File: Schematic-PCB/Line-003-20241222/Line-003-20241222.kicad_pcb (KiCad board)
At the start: 4 copper layers, 196 x 193.6 mm, 245 parts, among them J1 VIN, J2 Conn_MD, U47 LM393, U48 LM393, U49 LM393, U50 LM393, U51 LM393, U52 LM393, U53 LM393, U54 LM393, U55 LM393, U56 LM393, U57 LM393, U58 LM393, U59 LM393, U60 LM393, U61 LM393, U62 ATmega2560 Pro Board

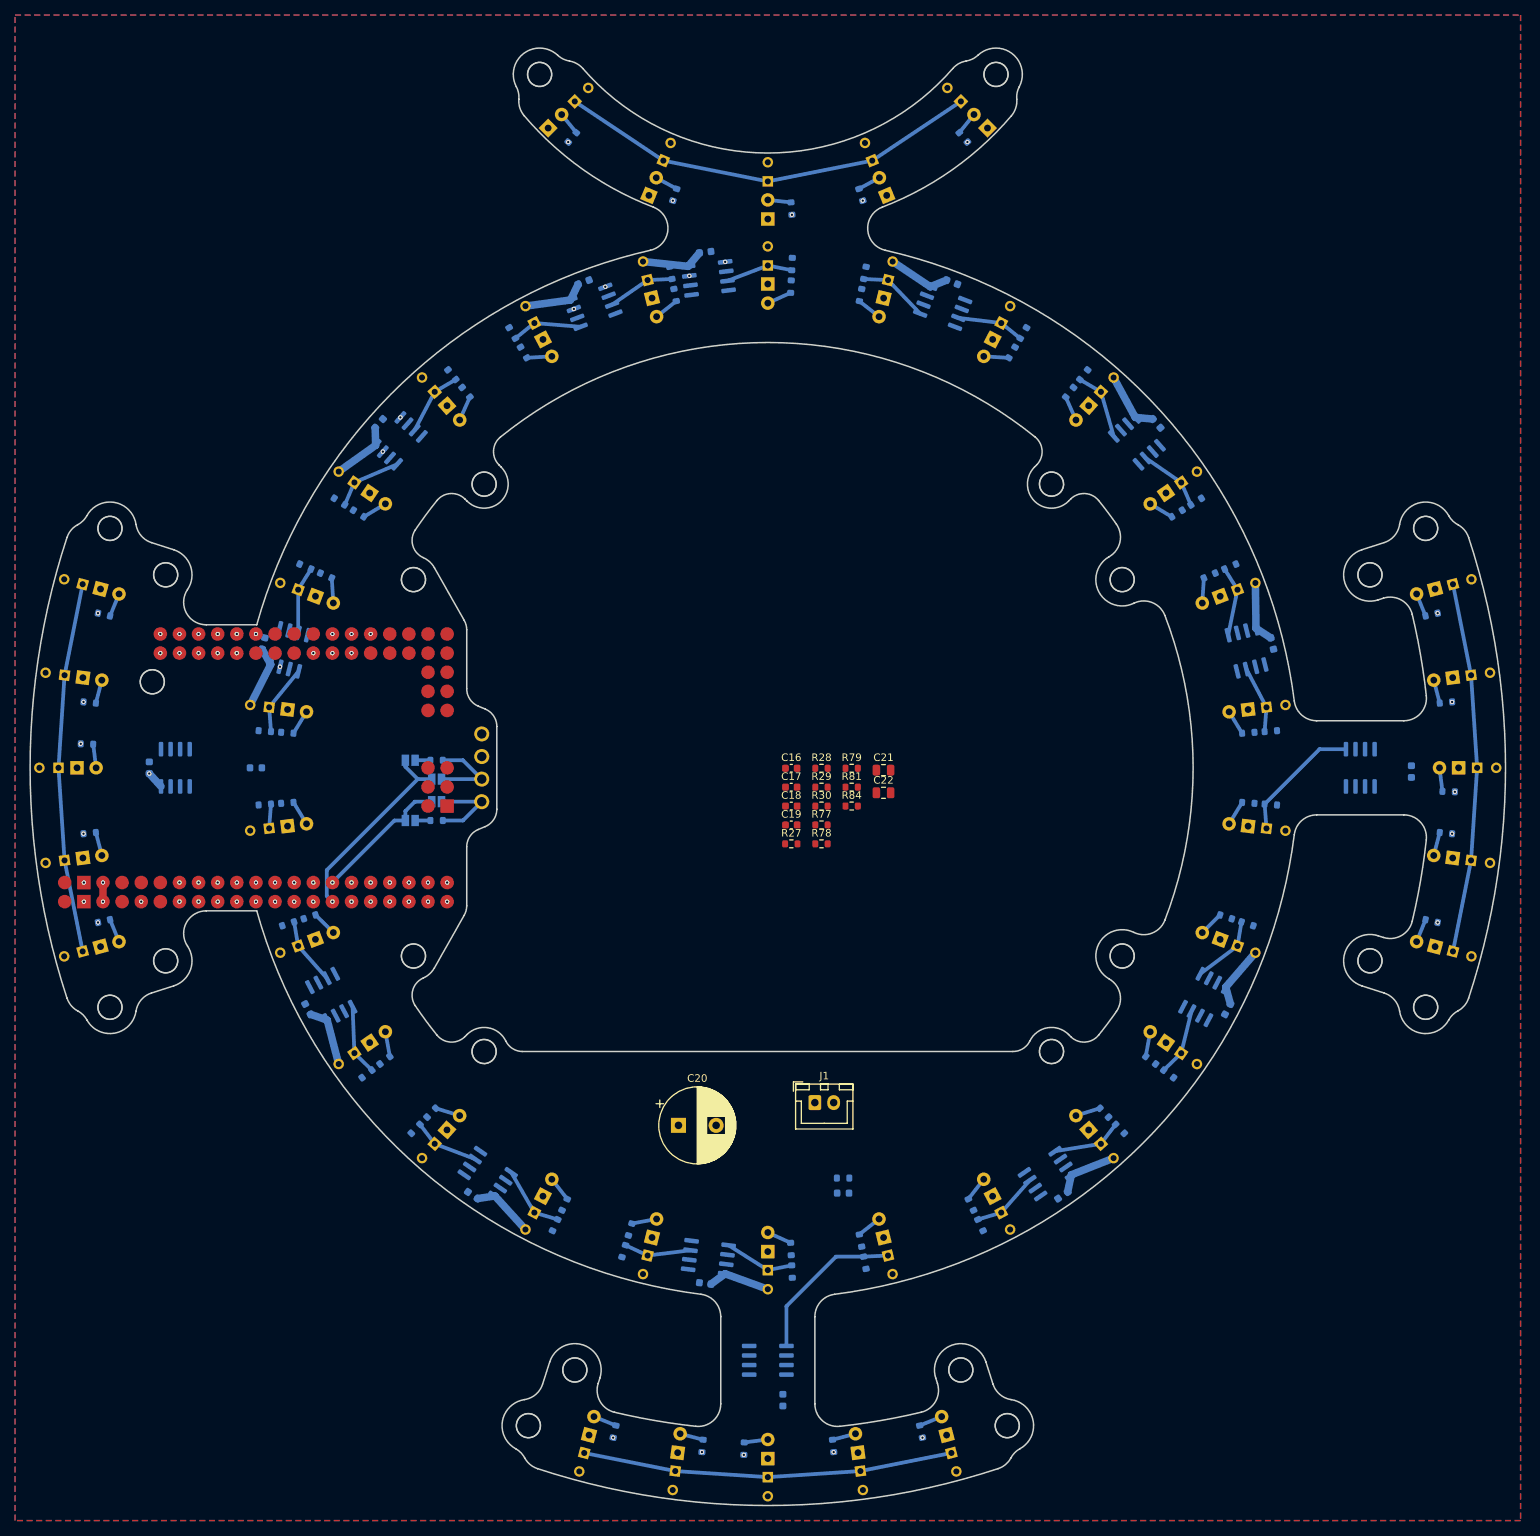
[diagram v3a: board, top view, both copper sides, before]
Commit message: update: ラインセンサ基板の基板外形を更新した
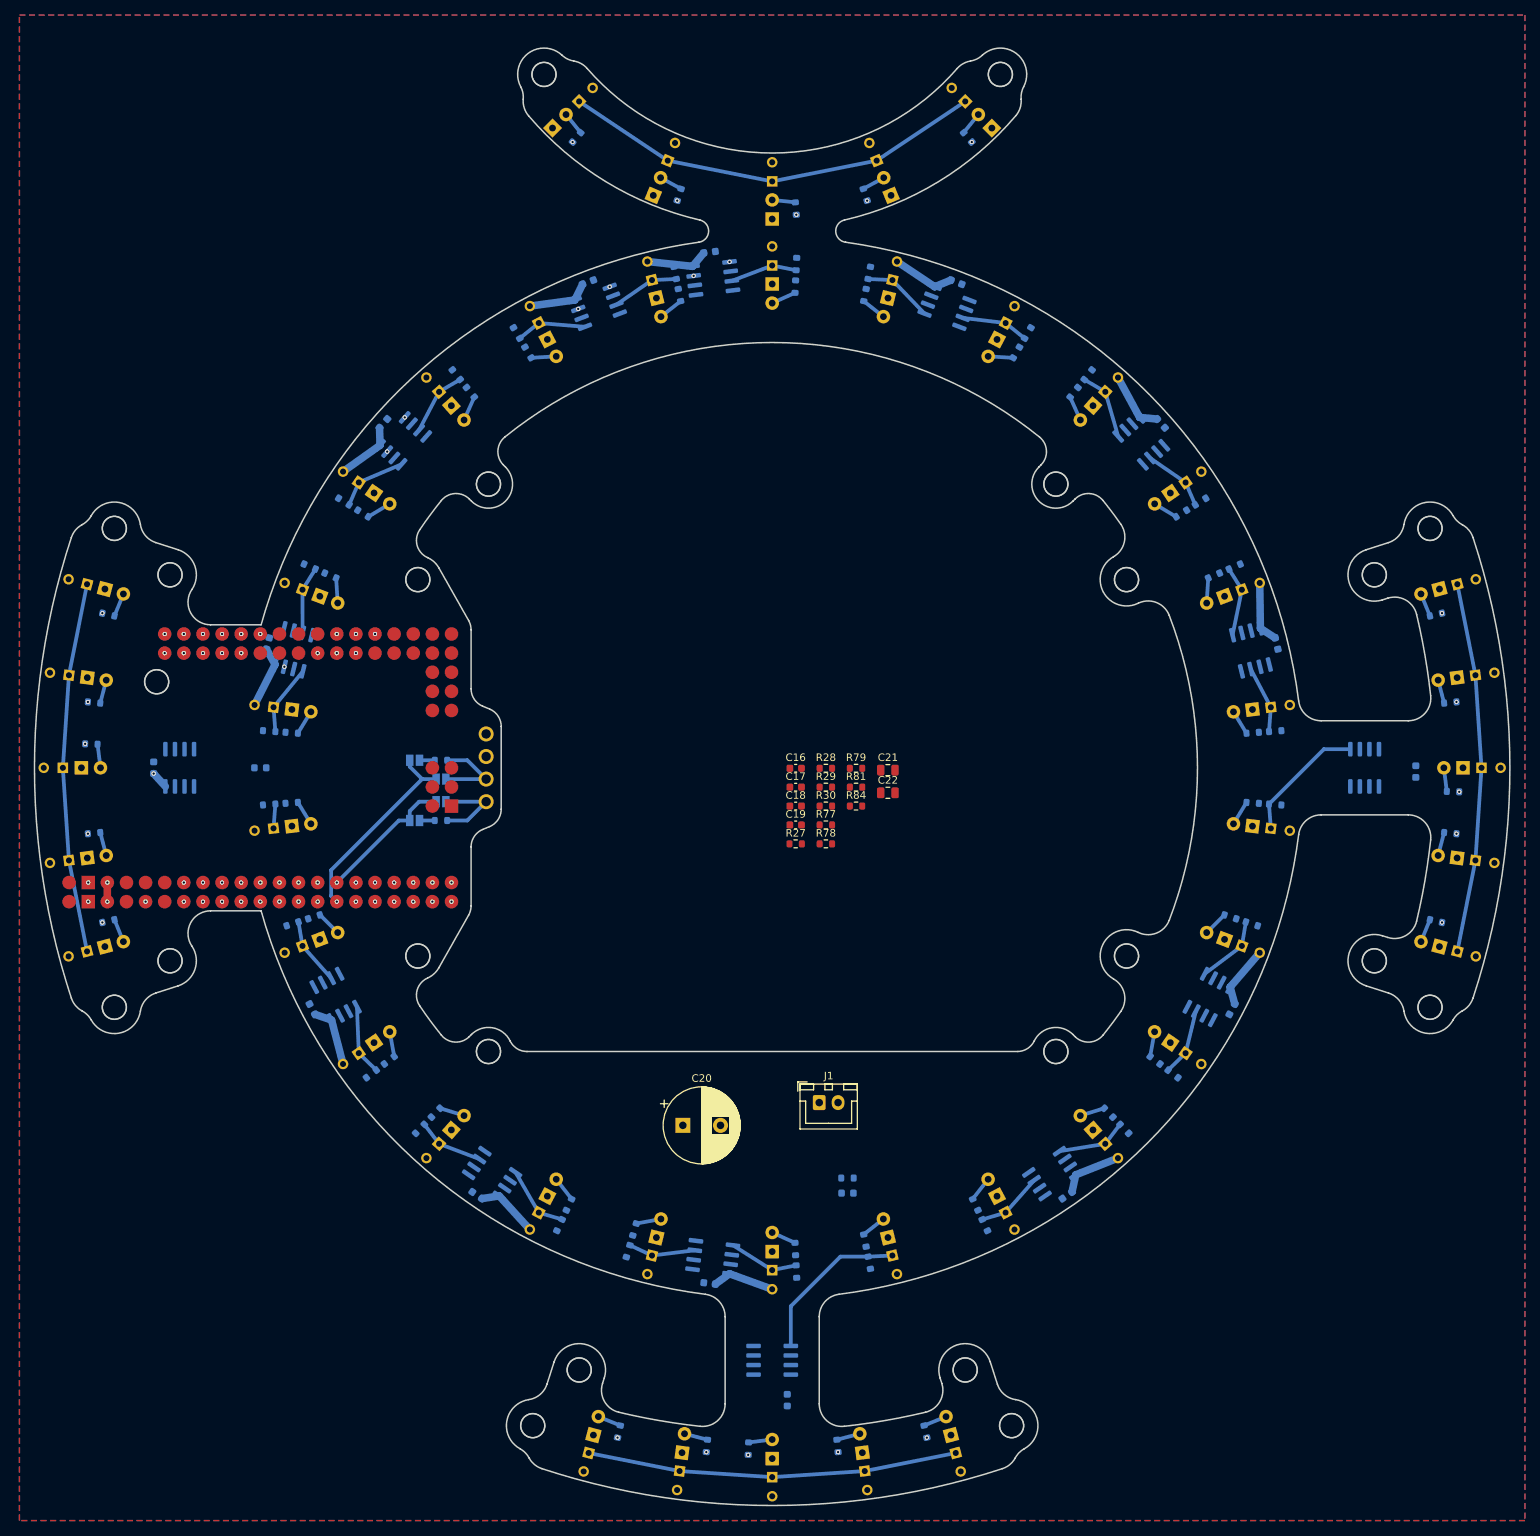
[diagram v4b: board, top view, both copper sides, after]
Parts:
- moved U26 0.58 mm to (16.3, -66.0)
- moved C10 0.58 mm to (67.0, -16.5)
- moved C11 0.58 mm to (51.7, -45.8)
- moved C13 0.58 mm to (-67.0, -16.5)
- moved C15 0.58 mm to (85.5, 0.50)
- moved C2 0.58 mm to (-24.5, -64.5)
- moved C21 0.58 mm to (15.4, 0.31)
- moved C22 0.58 mm to (15.4, 3.32)
- moved C3 0.58 mm to (-51.6, -45.8)
- moved C4 0.58 mm to (-82.2, -0.01)
- moved C5 0.58 mm to (-61.1, 32.1)
- moved C6 0.58 mm to (-39.2, 56.8)
- moved C7 0.58 mm to (-8.32, 68.5)
- moved C8 0.58 mm to (39.2, 56.8)
- moved C9 0.58 mm to (61.1, 32.1)
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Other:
- outline, holes or cut-outs redrawn

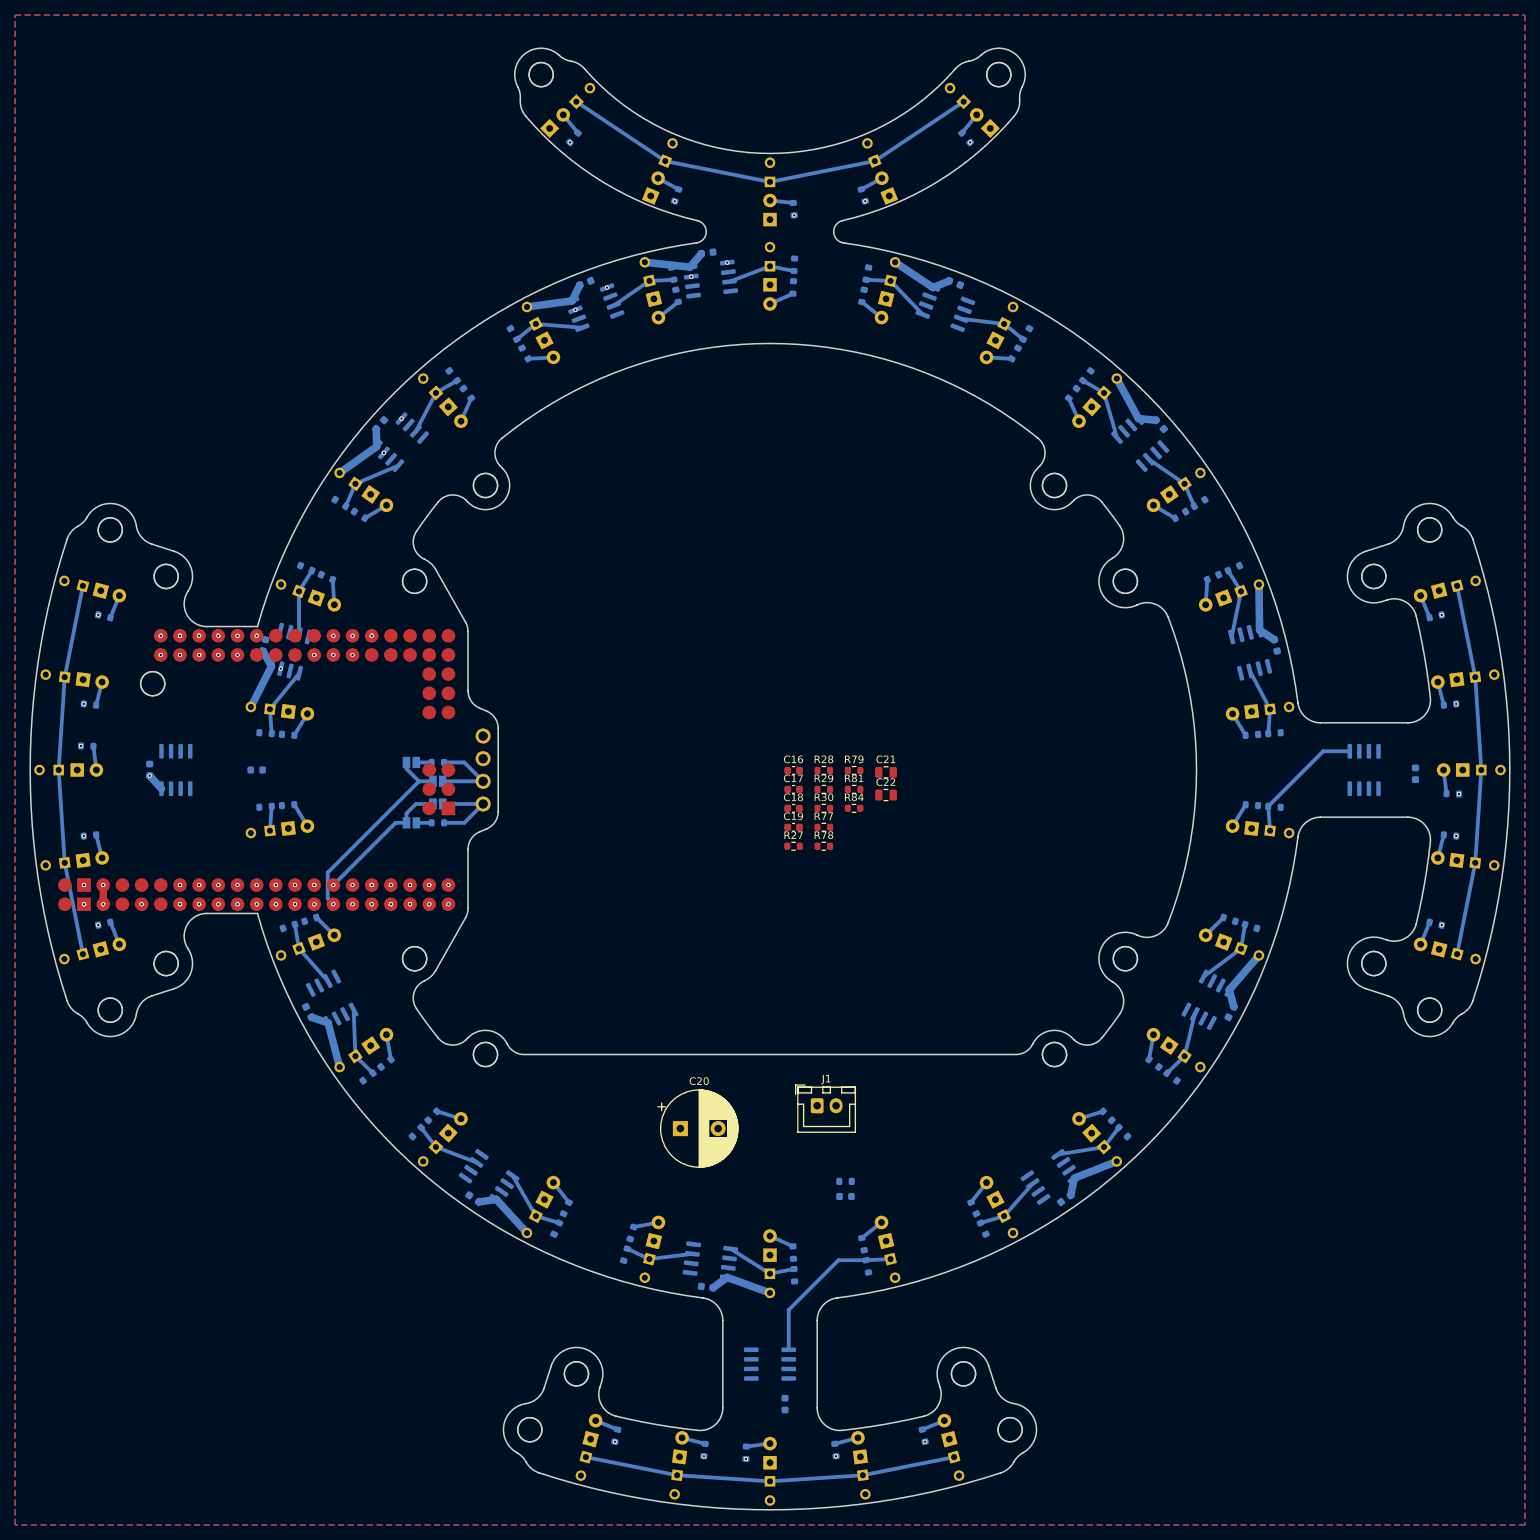
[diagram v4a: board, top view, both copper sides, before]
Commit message: update: ラインセンサ基板のPCBを更新した
部品配置はひととおりやったから配線を頼む
配線難しかったり逆に基板外形が大きすぎたらまた連絡して
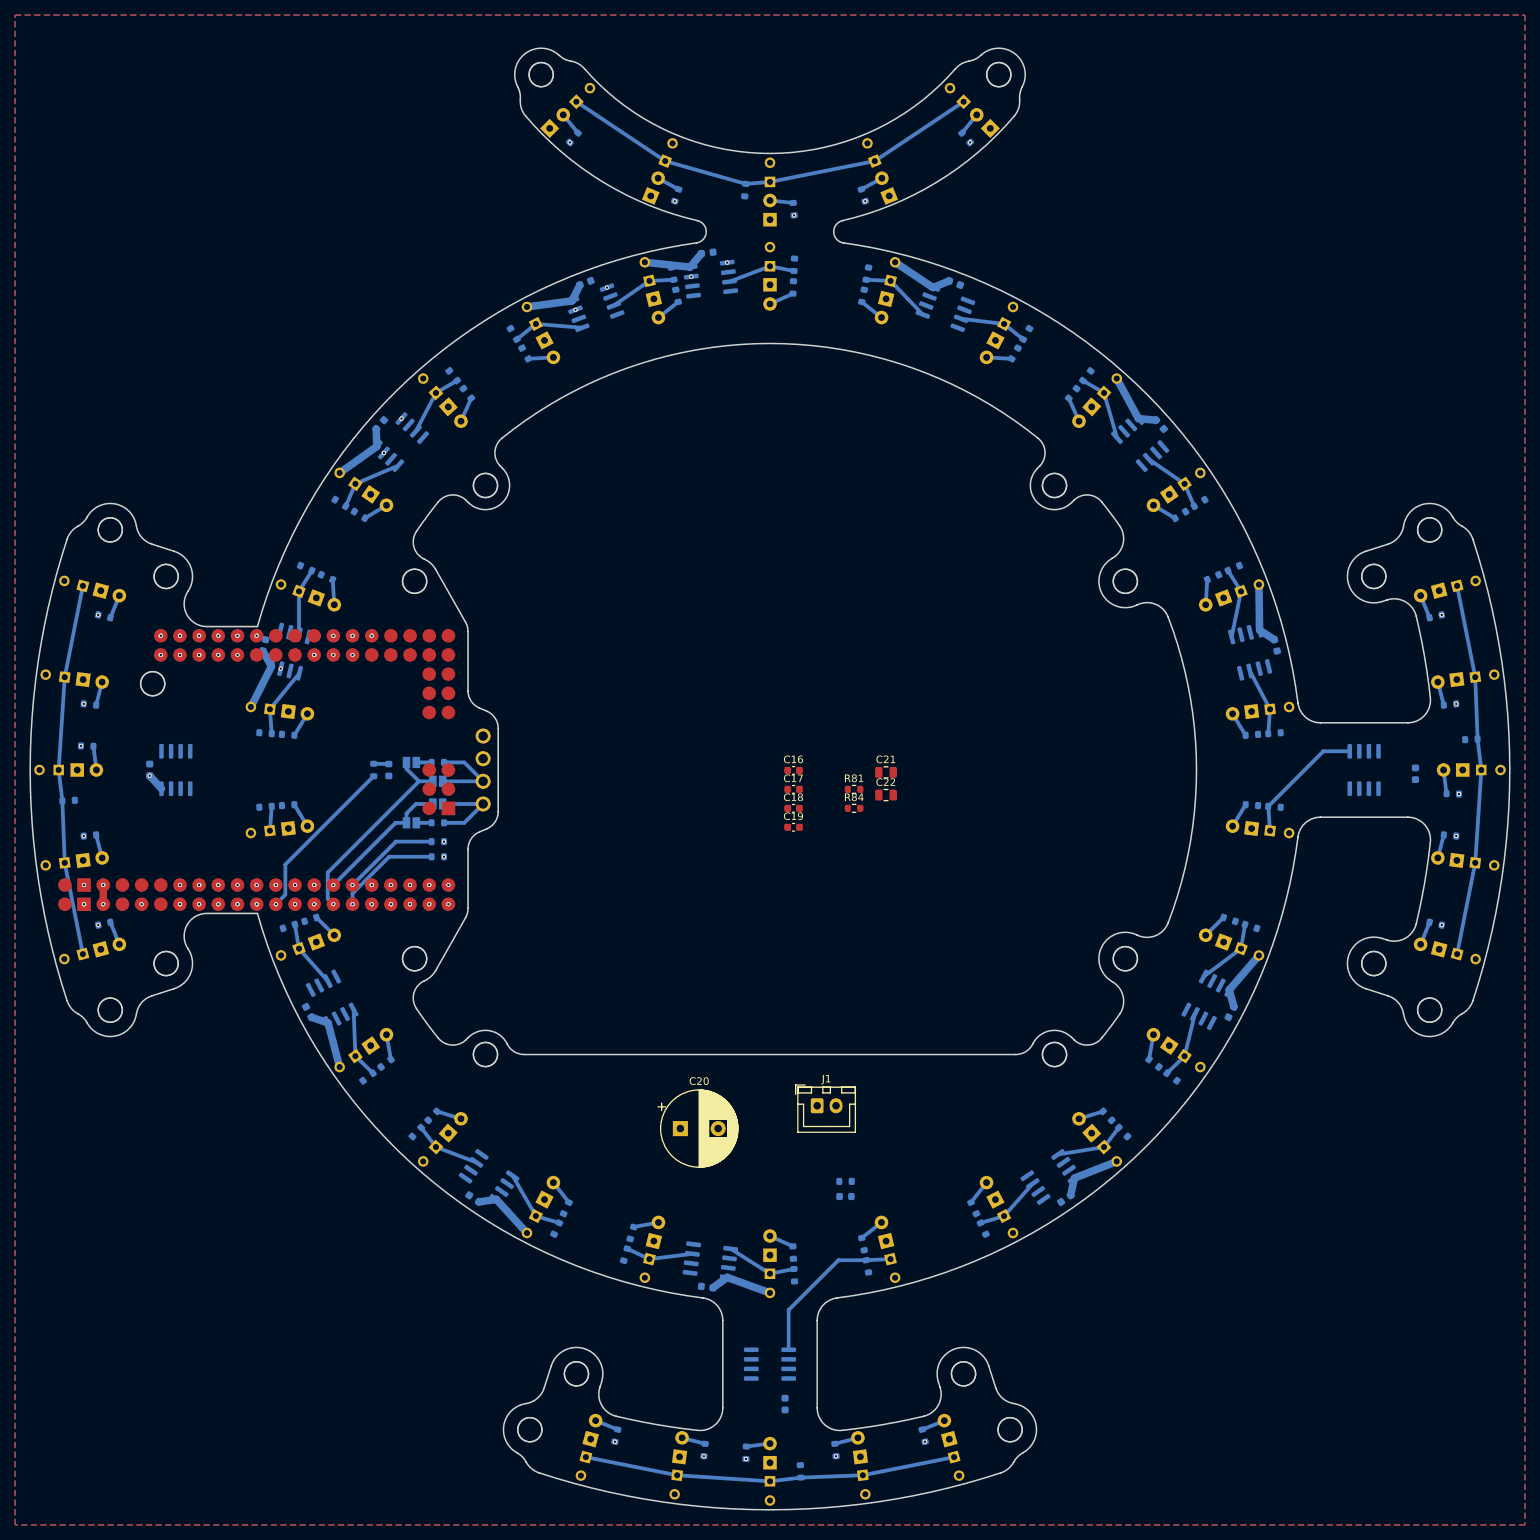
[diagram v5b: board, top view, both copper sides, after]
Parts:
- R27, R28, R29, R30, R77, R78, R79: moved to B.Cu
- moved R28 100.1 mm to (-92.9, 4.06), turned to 2.5 degrees
- moved R29 90.4 mm to (4.06, 92.9), turned to 92.5 degrees
- moved R27 87.1 mm to (-3.27, -76.8), turned to -95 degrees
- moved R30 86.3 mm to (92.9, -4.06), turned to -177.5 degrees
- moved R79 63.6 mm to (-52.5, 0.00), turned to 90 degrees
- moved R77 51.2 mm to (-44.0, 9.49), turned to 180 degrees
- moved R78 51.2 mm to (-44.0, 11.5), turned to 180 degrees
- moved D47 17.5 mm to (-50.5, 0.00), turned to 90 degrees
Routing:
- net LED_BUILTIN: track 0.00 -> 22.3 mm
- net SCL: track 0.00 -> 13.9 mm
- net SDA: track 0.00 -> 12.9 mm
- net Net-(D47-A): track 0.00 -> 2.00 mm
- net +5V: vias 23 -> 25
